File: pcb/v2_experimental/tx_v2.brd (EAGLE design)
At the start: 28 x 36.5 mm, 56 parts, among them IC1 STM32F030F4, IC2 NRF24L01ALT1, SW2 324_SW324_SWITCH_FOOT_HOLE, U2 USBC_16P, U3 MCP73831T-2ACI/OT, U4 XC6206_DEV, Y1 16MHz_12pF

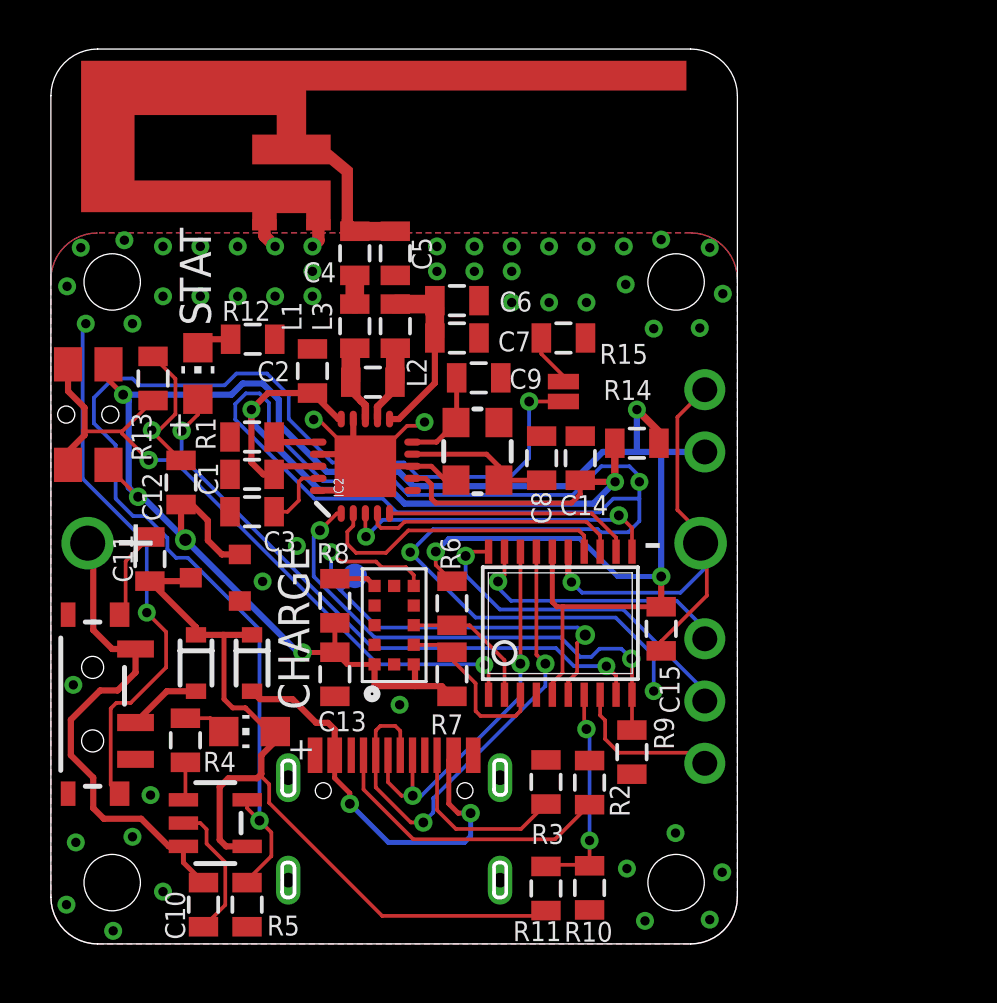
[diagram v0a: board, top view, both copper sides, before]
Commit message: new TX header with extra pin
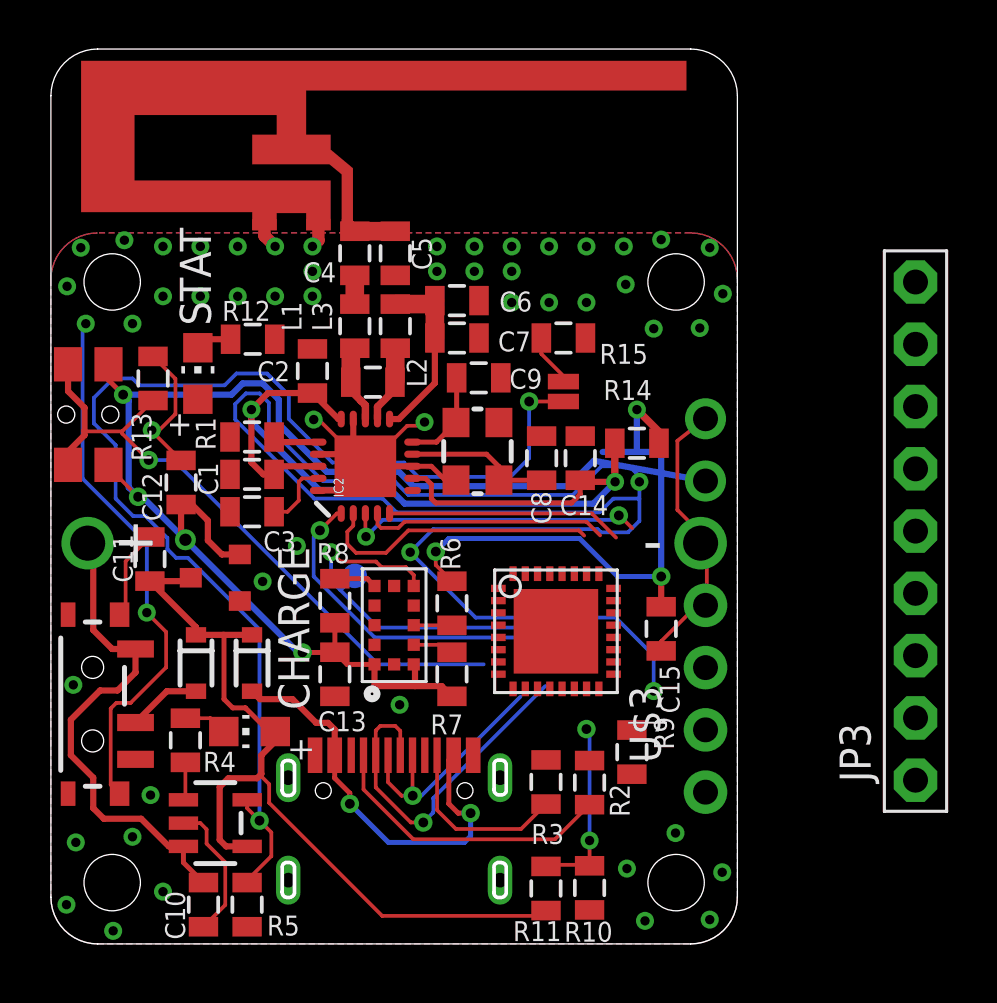
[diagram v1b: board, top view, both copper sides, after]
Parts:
- removed IC1: STM32F030F4, exixe_pogo:TSSOP20
- removed JP1: (no value), adafruit_changed:1X03-CLEANBIG
- added IC3: STM32L052K8U66, micro-stm:UFQFPN32
- added JP3: (no value), adafruit:1X09-BIG
- added U$3: PINHD1X4, adafruit_changed:1X04-CLEANBIG
- moved U$11 1.19 mm to (26.7, 20.1)
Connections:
- removed net N$22: IC1.3, R7.1, U1.10
- removed net N$23: IC1.2, R6.1, U1.9
- removed net N$29: IC1.9, LED2.A
- new net N$39: R7.1, U1.10
- new net N$40: R6.1, U1.9
- new net VDDA: IC3.5
- net +3V3: now also IC3.1, IC3.17; no longer IC1.16, IC1.5
- net GND: now also IC3.VSS; no longer IC1.15
- net N$14: no longer IC1.13
- net N$15: no longer IC1.12
- net N$16: no longer IC1.11
- net N$18: no longer IC1.18
- net N$20: no longer IC1.14
- net N$21: no longer IC1.10
- net N$30: no longer IC1.1
- net N$31: now also U$3.3; no longer IC1.19, JP1.3
- net N$32: now also U$3.2; no longer IC1.20, JP1.2
- net N$33: now also U$3.1; no longer IC1.8, JP1.1
- net N$34: no longer IC1.17
- net N$35: no longer IC1.7
- net N$36: no longer IC1.6
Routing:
- net N$29: track 24.8 -> 0.00 mm, vias 2 -> 0
- net N$32: track 13.9 -> 0.00 mm, vias 1 -> 0
- net N$31: track 11.1 -> 0.00 mm, vias 1 -> 0
- net GND: track 137.5 -> 128.9 mm, vias 57 -> 56
- net +3V3: track 90.2 -> 82.2 mm
- net N$22: track 7.14 -> 0.00 mm
- net N$21: track 20.7 -> 14.3 mm, vias 2 -> 1
- net N$33: track 6.37 -> 0.00 mm
- net N$18: track 16.0 -> 10.1 mm, vias 2 -> 1
- net N$23: track 5.70 -> 0.00 mm
- net N$34: track 20.3 -> 14.6 mm, vias 2 -> 1
- net N$36: track 20.2 -> 17.0 mm, vias 2 -> 1
- net N$39: track 0.00 -> 1.68 mm
- net N$40: track 0.00 -> 1.56 mm
- net N$30: track 28.0 -> 26.7 mm, vias 2 -> 1
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
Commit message: hooked up new MCU
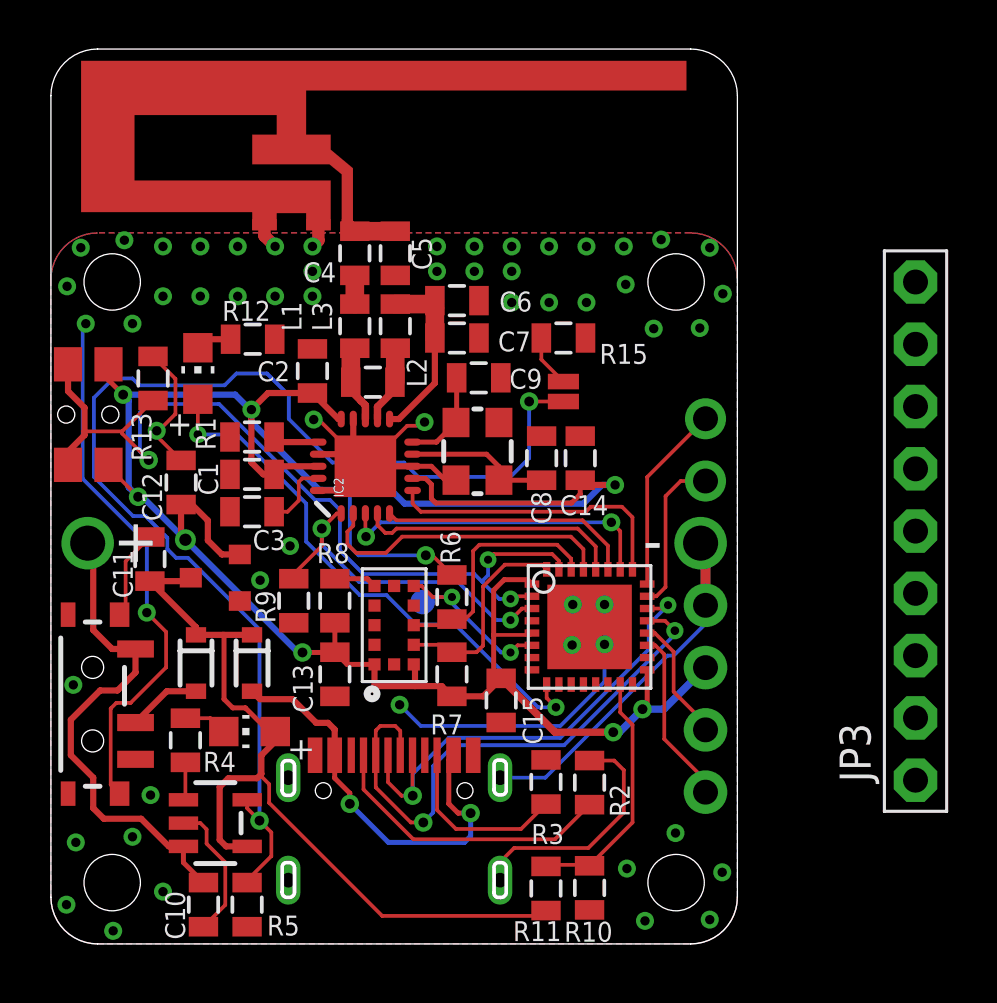
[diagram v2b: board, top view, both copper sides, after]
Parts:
- removed R14: 1 Ohm, joyAnalog:0805
- moved R9 15.1 mm to (9.91, 14.0)
- moved C15 7.15 mm to (18.4, 9.93)
- moved TP2 2.97 mm to (15.2, 13.9)
- moved IC3 1.38 mm to (22.0, 12.9)
- moved R6 0.25 mm to (16.4, 14.1)
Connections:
- removed net N$33: U$3.1
- removed net N$34: U2.A7, U2.B7
- removed net N$37: C1.1, C14.1, C2.1, IC2.15, IC2.18, IC2.7, R14.2
- removed net VDDA: IC3.5
- new net N$22: IC2.6, IC3.25
- new net N$23: IC3.9, LED2.A
- new net N$29: IC3.23, U$11.1
- new net USB_DM: IC3.21, U2.A7, U2.B7
- new net USB_DP: IC3.22, U2.A6, U2.B6
- net +3V3: now also C1.1, C14.1, C2.1, IC2.15, IC2.18, IC2.7, IC3.5, U$3.3; no longer R14.1, U$11.1
- net GND: now also U$3.4; no longer U$11.2
- net N$14: now also IC3.28
- net N$15: now also IC3.27
- net N$16: now also IC3.26
- net N$18: now also IC3.24, U$11.2; no longer U2.A6, U2.B6
- net N$20: now also IC3.29
- net N$21: now also IC3.3
- net N$30: now also IC3.2, IC3.31
- net N$31: now also IC3.20, U$3.2; no longer U$3.3
- net N$32: now also IC3.19, U$3.1; no longer U$3.2
- net N$35: now also IC3.15
- net N$36: now also IC3.6
- net N$39: now also IC3.32
- net N$40: now also IC3.30
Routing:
- net N$37: track 38.0 -> 0.00 mm, vias 2 -> 0
- net GND: track 128.9 -> 91.9 mm, vias 56 -> 57
- net USB_DM: track 0.00 -> 23.0 mm, vias 0 -> 2
- net N$23: track 0.00 -> 22.6 mm, vias 0 -> 2
- net +3V3: track 82.2 -> 102.1 mm, vias 7 -> 9
- net USB_DP: track 0.00 -> 19.6 mm, vias 0 -> 2
- net N$34: track 14.6 -> 0.00 mm, vias 1 -> 0
- net N$22: track 0.00 -> 12.0 mm
- net N$30: track 26.7 -> 36.5 mm, vias 1 -> 3
- net N$36: track 17.0 -> 7.49 mm, vias 1 -> 2
- net N$40: track 1.56 -> 9.89 mm
- net N$32: track 0.00 -> 7.17 mm
- net N$39: track 1.68 -> 8.52 mm
- net N$29: track 0.00 -> 6.50 mm
- net N$31: track 0.00 -> 5.12 mm
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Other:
- board text added: "+"
- board text added: "G"
- board text added: "RX"
- board text removed: "CHARGE"
- board text removed: "GND"
- board text removed: "STAT"

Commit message: added switch cutout and testpads
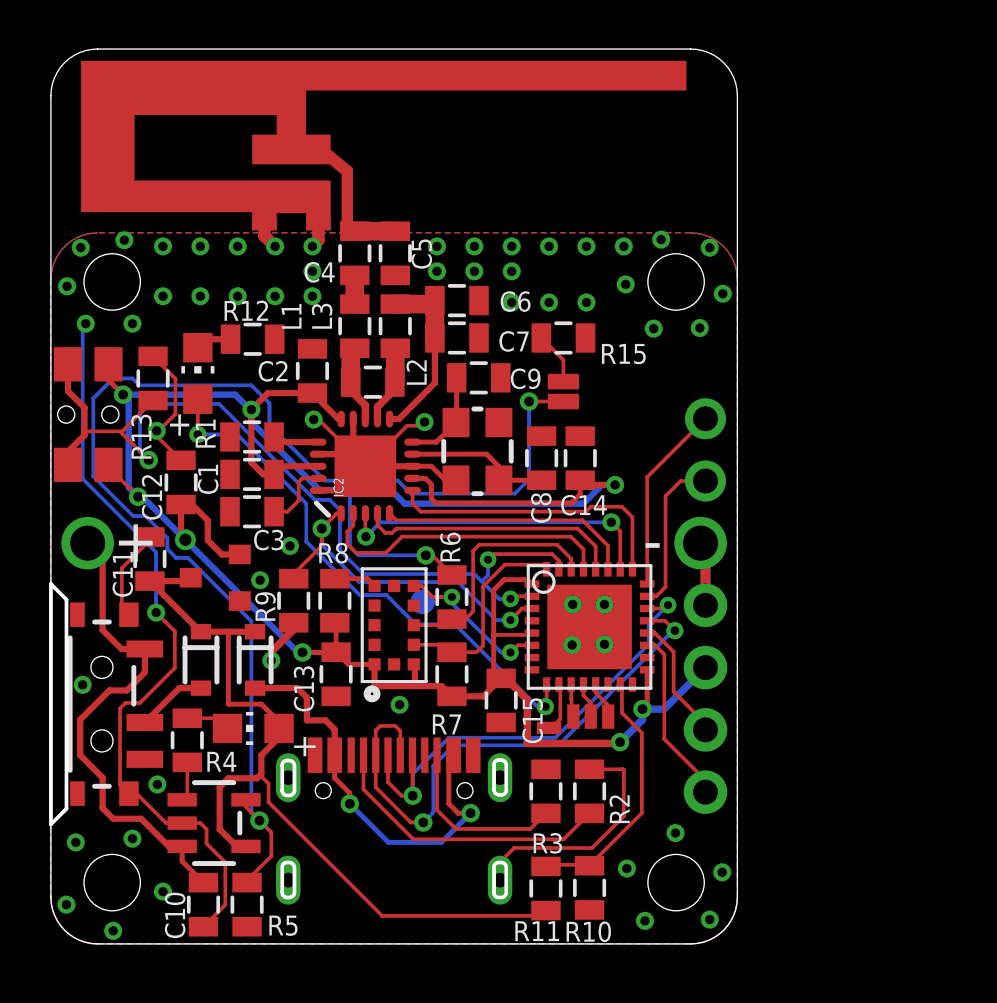
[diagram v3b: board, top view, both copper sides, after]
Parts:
- removed JP3: (no value), adafruit:1X09-BIG
- added U$4, U$5, U$6, U$7: TESTPAD, micro-stm:TESTPAD
- moved R3 0.38 mm to (20.2, 6.22)
- moved SW1 0.38 mm to (2.08, 9.78)
- moved R2 0.36 mm to (22.0, 6.22)
- moved D2 0.24 mm to (6.12, 11.6)
- moved LED1 0.20 mm to (8.26, 8.79)
- moved D1 0.18 mm to (8.33, 11.6)
- moved R4 0.08 mm to (5.56, 8.31)
- moved C13 0.05 mm to (11.6, 11.0)
- moved U3 0.05 mm to (6.65, 4.93)
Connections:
- new net N$33: IC3.10, U$5.P$1
- new net N$34: IC3.11, U$4.P$1
- new net N$37: IC3.12, U$7.P$1
- new net N$41: IC3.13, U$6.P$1
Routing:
- net GND: track 91.9 -> 74.7 mm, vias 57 -> 58
- net N$33: track 0.00 -> 2.04 mm
- net +3V3: track 102.1 -> 103.8 mm
- net N$41: track 0.00 -> 1.52 mm
- net N$37: track 0.00 -> 1.43 mm
- net N$34: track 0.00 -> 1.34 mm
- net N$17: track 49.6 -> 50.2 mm
- net N$23: track 22.6 -> 22.0 mm
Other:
- outline, holes or cut-outs redrawn
